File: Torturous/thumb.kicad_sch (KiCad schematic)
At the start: 3 parts, among them J2 Conn_01x04_Pin

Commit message: started the phys layout
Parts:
- J2: footprint (none) -> Connector_FFC-FPC:Amphenol_F32Q-1A7x1-11004_1x04-1MP_P0.5mm_Horizontal
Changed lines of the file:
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@@
 			)
 		)
-		(property "Footprint" ""
+		(property "Footprint" "Connector_FFC-FPC:Amphenol_F32Q-1A7x1-11004_1x04-1MP_P0.5mm_Horizontal"
 			(at 100.33 63.5 0)
 			(hide yes)

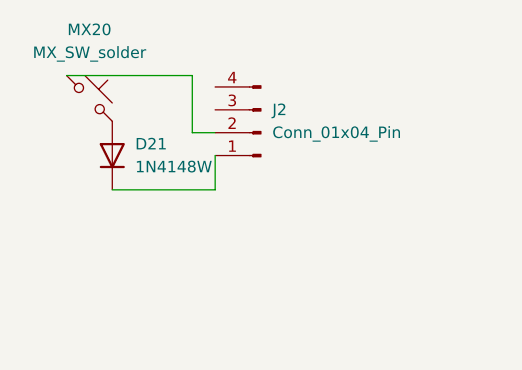
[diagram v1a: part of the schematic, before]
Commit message: routing finnished for the main board
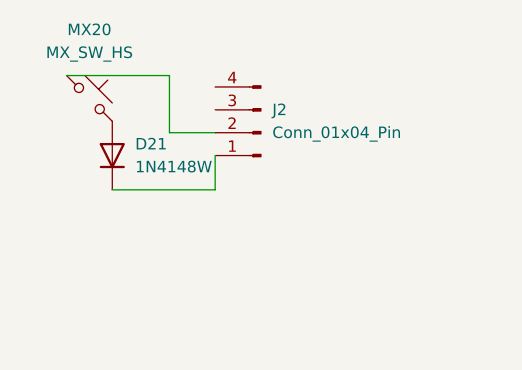
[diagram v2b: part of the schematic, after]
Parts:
- removed MX20: MX_SW_solder, PCM_marbastlib-mx:SW_MX_1u, symbol PCM_marbastlib-mx:MX_SW_solder
- added MX20: MX_SW_HS, PCM_marbastlib-mx:SW_MX_HS_CPG151101S11_1u, symbol PCM_marbastlib-mx:MX_SW_HS_CPG151101S11
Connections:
- net at J2.2 (Pin_2): now also MX20.1
- net at D21.2 (A): now also MX20.2
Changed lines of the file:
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@@
 	(wire
 		(pts
-			(xy 92.71 63.5) (xy 95.25 63.5)
+			(xy 90.17 63.5) (xy 95.25 63.5)
 		)
 		(stroke
@@
 	(wire
 		(pts
-			(xy 92.71 57.15) (xy 92.71 63.5)
-		)
-		(stroke
-			(width 0)
-			(type default)
-		)
-	)
-	(wire
-		(pts
-			(xy 78.74 57.15) (xy 92.71 57.15)
+			(xy 90.17 57.15) (xy 90.17 63.5)
+		)
+		(stroke
+			(width 0)
+			(type default)
+		)
+	)
+	(wire
+		(pts
+			(xy 78.74 57.15) (xy 90.17 57.15)
 		)
 		(stroke
@@
 			(width 0)
 			(type default)
-		)
-	)
-	(symbol
-		(lib_id "PCM_marbastlib-mx:MX_SW_solder")
-		(at 81.28 59.69 0)
-		(unit 1)
-		(body_style 1)
-		(exclude_from_sim no)
-		(in_bom yes)
-		(on_board yes)
-		(in_pos_files yes)
-		(dnp no)
-		(fields_autoplaced yes)
-		(property "Reference" "MX20"
-			(at 81.28 52.07 0)
-			(show_name no)
-			(do_not_autoplace no)
-			(effects
-				(font
-					(size 1.27 1.27)
-				)
-			)
-		)
-		(property "Value" "MX_SW_solder"
-			(at 81.28 54.61 0)
-			(show_name no)
-			(do_not_autoplace no)
-			(effects
-				(font
-					(size 1.27 1.27)
-				)
-			)
-		)
-		(property "Footprint" "PCM_marbastlib-mx:SW_MX_1u"
-			(at 81.28 59.69 0)
-			(hide yes)
-			(show_name no)
-			(do_not_autoplace no)
-			(effects
-				(font
-					(size 1.27 1.27)
-				)
-			)
-		)
-		(property "Datasheet" ""
-			(at 81.28 59.69 0)
-			(hide yes)
-			(show_name no)
-			(do_not_autoplace no)
-			(effects
-				(font
-					(size 1.27 1.27)
-				)
-			)
-		)
-		(property "Description" "Push button switch, normally open, two pins, 45° tilted"
-			(at 81.28 59.69 0)
-			(hide yes)
-			(show_name no)
-			(do_not_autoplace no)
-			(effects
-				(font
-					(size 1.27 1.27)
-				)
-			)
-		)
-		(pin "2"
-		)
-		(pin "1"
-		)
-		(instances
-			(project "Torturous"
-				(path "/ff534fae-ff9f-4407-93f5-4b7919801e88/055095fa-150c-4686-ad88-cfbdebbe6e43"
-					(reference "MX20")
-					(unit 1)
-				)
-			)
 		)
 	)
@@
 					(unit 1)
 				)
+			)
+		)
+	)
+	(symbol
+		(lib_id "PCM_marbastlib-mx:MX_SW_HS_CPG151101S11")
+		(at 81.28 59.69 0)
+		(unit 1)
+		(body_style 1)
+		(exclude_from_sim no)
+		(in_bom yes)
+		(on_board yes)
+		(in_pos_files yes)
+		(dnp no)
+		(fields_autoplaced yes)
+		(property "Reference" "MX20"
+			(at 81.28 52.07 0)
+			(show_name no)
+			(do_not_autoplace no)
+			(effects
+				(font
+					(size 1.27 1.27)
+				)
+			)
+		)
+		(property "Value" "MX_SW_HS"
+			(at 81.28 54.61 0)
+			(show_name no)
+			(do_not_autoplace no)
+			(effects
+				(font
+					(size 1.27 1.27)
+				)
+			)
+		)
+		(property "Footprint" "PCM_marbastlib-mx:SW_MX_HS_CPG151101S11_1u"
+			(at 81.28 59.69 0)
+			(hide yes)
+			(show_name no)
+			(do_not_autoplace no)
+			(effects
+				(font
+					(size 1.27 1.27)
+				)
+			)
+		)
+		(property "Datasheet" ""
+			(at 81.28 59.69 0)
+			(hide yes)
+			(show_name no)
+			(do_not_autoplace no)
+			(effects
+				(font
+					(size 1.27 1.27)
+				)
+			)
+		)
+		(property "Description" "Push button switch, normally open, two pins, 45° tilted, Kailh CPG151101S11 for Cherry MX style switches"
+			(at 81.28 59.69 0)
+			(hide yes)
+			(show_name no)
+			(do_not_autoplace no)
+			(effects
+				(font
+					(size 1.27 1.27)
+				)
+			)
+		)
+		(pin "2"
+		)
+		(pin "1"
+		)
+		(instances
+			(project "Torturous"
+				(path "/ff534fae-ff9f-4407-93f5-4b7919801e88/055095fa-150c-4686-ad88-cfbdebbe6e43"
+					(reference "MX20")
+					(unit 1)
+				)
